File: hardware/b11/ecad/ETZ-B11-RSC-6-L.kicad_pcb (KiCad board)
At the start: 2 copper layers, 131.5 x 85.8 mm, 44 parts, among them SW1 Kailh_socket_PG1350, SW10 Kailh_socket_PG1350, SW11 Kailh_socket_PG1350, SW12 Kailh_socket_PG1350, SW13 Kailh_socket_PG1350, SW14 Kailh_socket_PG1350, SW15 Kailh_socket_PG1350, SW16 Kailh_socket_PG1350, SW17 Kailh_socket_PG1350, SW18 Kailh_socket_PG1350, SW19 Kailh_socket_PG1350, SW2 Kailh_socket_PG1350, SW20 Kailh_socket_PG1350, SW21 Kailh_socket_PG1350, SW22 Kailh_socket_PG1350, SW3 Kailh_socket_PG1350, SW4 Kailh_socket_PG1350, SW5 Kailh_socket_PG1350, SW6 Kailh_socket_PG1350, SW7 Kailh_socket_PG1350, SW8 Kailh_socket_PG1350, SW9 Kailh_socket_PG1350

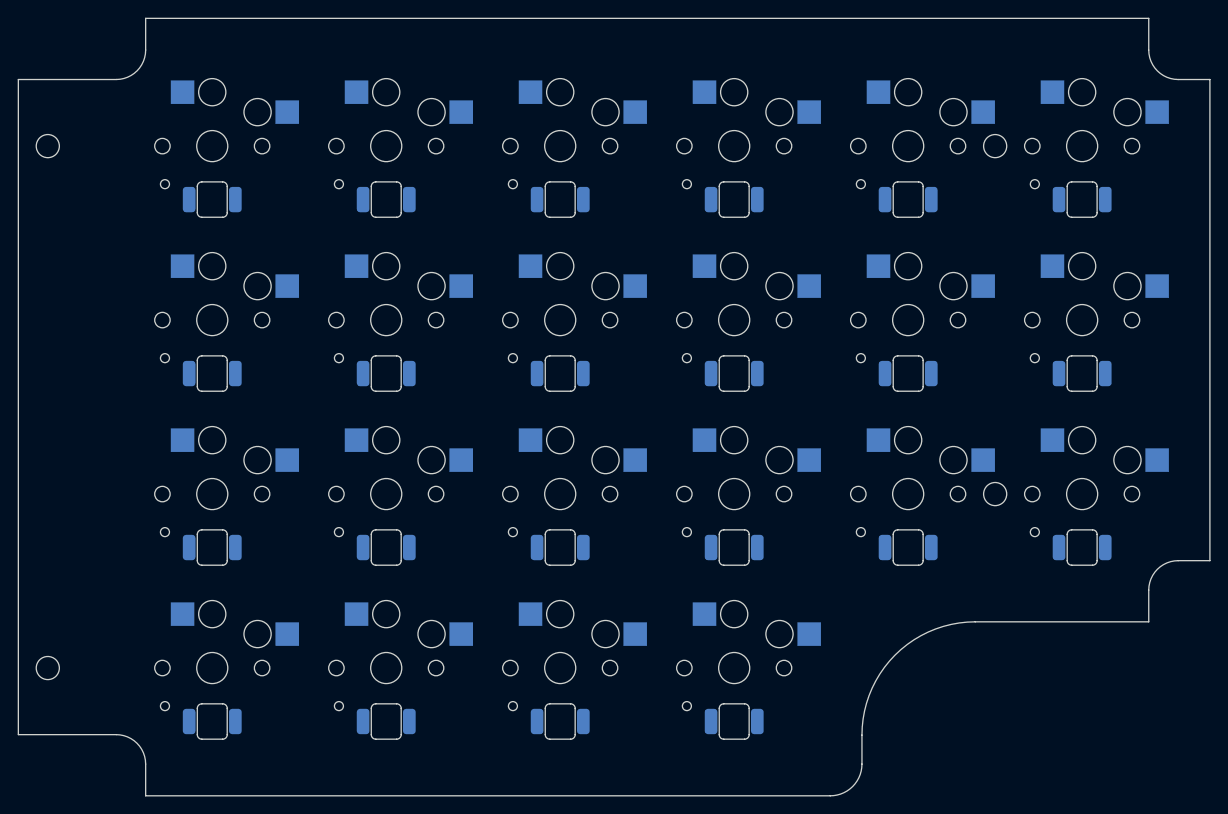
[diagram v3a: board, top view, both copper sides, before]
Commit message: fix(hardware/b11): fix switch socket placement, 3D models, and submodule pins
- Pin MX_V2 submodule to ab59b57 (before upstream "topside pads" change that
  moved SMD pads to F.Cu — old commit has correct B.Cu pads natively)
- Fix SWIG type-registry corruption in both switch placement scripts by
  pre-loading all footprint instances and caching pad refs before LoadBoard()
- Fix LP script: add make_patched_lib to rewrite Choc socket 3D model path
  to absolute path and convert old (at ...) inch offset to (offset ...) mm
  format — KiCad 9 was multiplying the old format by 25.4, placing model
  127mm off-center
- Regenerate all 8 carrier PCBs with updated board outlines (LSC-6 mounting
  hole positions) and correctly placed switches + LEDs

Co-Authored-By: Claude Sonnet 4.6 <noreply@anthropic.com>
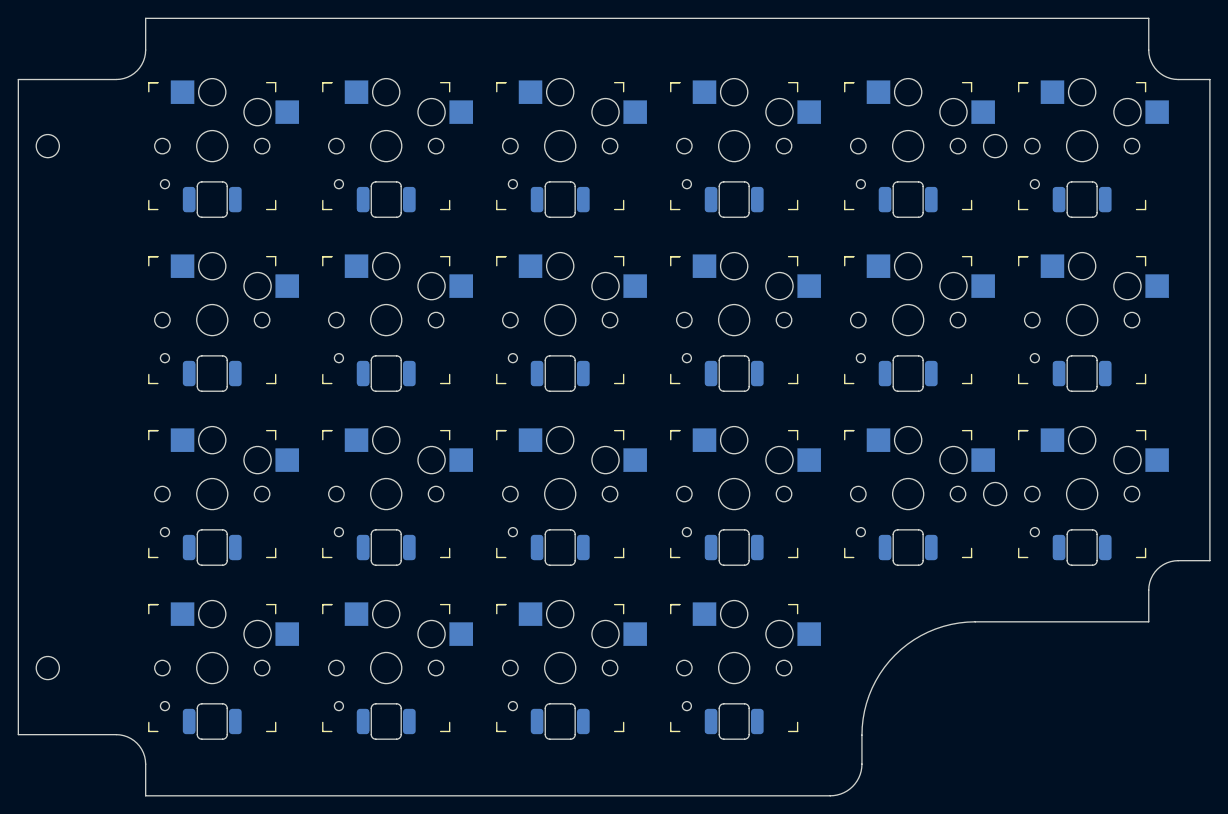
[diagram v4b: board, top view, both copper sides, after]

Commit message: fix(hardware/b11): adjust LED offset to 5.0mm and regenerate all carrier PCBs
Reduces south-facing LED offset from 5.9mm to 5.0mm (closer to the
standard 5.08mm switch-to-LED spacing). All 8 carrier PCBs regenerated.

Co-Authored-By: Claude Sonnet 4.6 <noreply@anthropic.com>
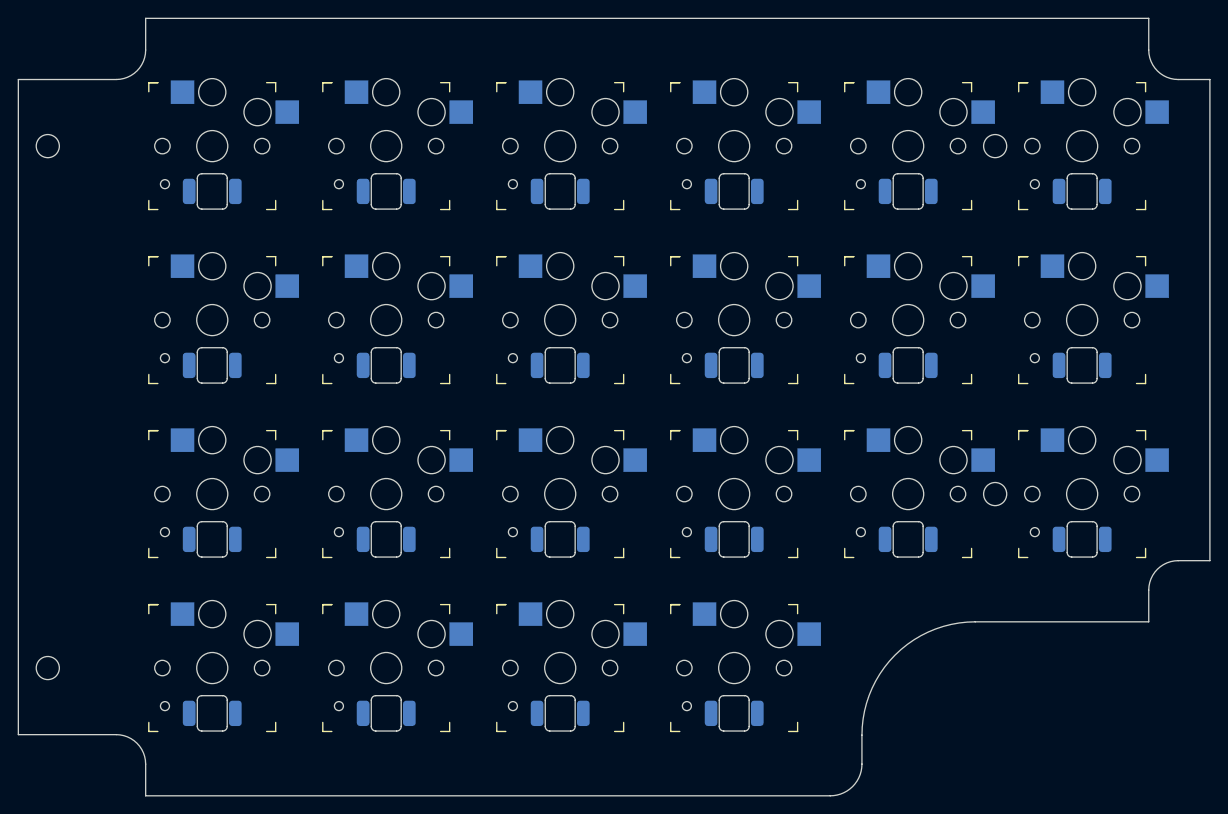
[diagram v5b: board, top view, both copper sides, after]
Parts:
- moved LED13 0.90 mm to (200.2, 116.7)
- moved LED14 0.90 mm to (180.9, 116.7)
- moved LED15 0.90 mm to (161.8, 116.7)
- moved LED16 0.90 mm to (142.6, 116.7)
- moved LED17 0.90 mm to (123.3, 116.7)
- moved LED18 0.90 mm to (104.2, 116.7)
- moved LED1 0.90 mm to (200.2, 78.3)
- moved LED10 0.90 mm to (142.6, 97.5)
- moved LED11 0.90 mm to (123.3, 97.5)
- moved LED12 0.90 mm to (104.2, 97.5)
- moved LED19 0.90 mm to (161.8, 135.9)
- moved LED2 0.90 mm to (180.9, 78.3)
- moved LED20 0.90 mm to (142.6, 135.9)
- moved LED21 0.90 mm to (123.3, 135.9)
- moved LED22 0.90 mm to (104.2, 135.9)
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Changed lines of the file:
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@@
 	(footprint "LED_SMD_6028_BackMount"
 		(layer "B.Cu")
-		(at 142.55 79.2)
+		(at 104.15 116.699999)
 		(descr "SMD 6028 back-paste reverse-mount LED, 5.88x2.80mm body, 3.20mm lens, slot 3.3x6.2mm")
 		(tags "LED SMD 6028 reverse-mount back-paste backlighting Choc")
-		(property "Reference" "LED4"
+		(property "Reference" "LED18"
 			(at 0 -2 0)
 			(layer "B.Fab")
@@
 	(footprint "LED_SMD_6028_BackMount"
 		(layer "B.Cu")
-		(at 200.15 98.4)
+		(at 200.15 97.5)
 		(descr "SMD 6028 back-paste reverse-mount LED, 5.88x2.80mm body, 3.20mm lens, slot 3.3x6.2mm")
 		(tags "LED SMD 6028 reverse-mount back-paste backlighting Choc")
@@
 	(footprint "LED_SMD_6028_BackMount"
 		(layer "B.Cu")
-		(at 123.35 117.6)
+		(at 161.75 116.699999)
 		(descr "SMD 6028 back-paste reverse-mount LED, 5.88x2.80mm body, 3.20mm lens, slot 3.3x6.2mm")
 		(tags "LED SMD 6028 reverse-mount back-paste backlighting Choc")
-		(property "Reference" "LED17"
+		(property "Reference" "LED15"
 			(at 0 -2 0)
 			(layer "B.Fab")
@@
 	(footprint "LED_SMD_6028_BackMount"
 		(layer "B.Cu")
-		(at 200.15 117.6)
+		(at 142.55 135.899999)
 		(descr "SMD 6028 back-paste reverse-mount LED, 5.88x2.80mm body, 3.20mm lens, slot 3.3x6.2mm")
 		(tags "LED SMD 6028 reverse-mount back-paste backlighting Choc")
-		(property "Reference" "LED13"
+		(property "Reference" "LED20"
 			(at 0 -2 0)
 			(layer "B.Fab")
@@
 	(footprint "LED_SMD_6028_BackMount"
 		(layer "B.Cu")
-		(at 180.95 98.4)
+		(at 161.75 78.3)
 		(descr "SMD 6028 back-paste reverse-mount LED, 5.88x2.80mm body, 3.20mm lens, slot 3.3x6.2mm")
 		(tags "LED SMD 6028 reverse-mount back-paste backlighting Choc")
-		(property "Reference" "LED8"
+		(property "Reference" "LED3"
 			(at 0 -2 0)
 			(layer "B.Fab")
@@
 	(footprint "LED_SMD_6028_BackMount"
 		(layer "B.Cu")
-		(at 123.35 98.4)
+		(at 161.75 97.5)
 		(descr "SMD 6028 back-paste reverse-mount LED, 5.88x2.80mm body, 3.20mm lens, slot 3.3x6.2mm")
 		(tags "LED SMD 6028 reverse-mount back-paste backlighting Choc")
-		(property "Reference" "LED11"
+		(property "Reference" "LED9"
 			(at 0 -2 0)
 			(layer "B.Fab")
@@
 	(footprint "LED_SMD_6028_BackMount"
 		(layer "B.Cu")
-		(at 104.15 136.799999)
+		(at 123.35 135.899999)
 		(descr "SMD 6028 back-paste reverse-mount LED, 5.88x2.80mm body, 3.20mm lens, slot 3.3x6.2mm")
 		(tags "LED SMD 6028 reverse-mount back-paste backlighting Choc")
-		(property "Reference" "LED22"
+		(property "Reference" "LED21"
 			(at 0 -2 0)
 			(layer "B.Fab")
@@
 	(footprint "LED_SMD_6028_BackMount"
 		(layer "B.Cu")
-		(at 142.55 117.6)
+		(at 104.15 135.899999)
 		(descr "SMD 6028 back-paste reverse-mount LED, 5.88x2.80mm body, 3.20mm lens, slot 3.3x6.2mm")
 		(tags "LED SMD 6028 reverse-mount back-paste backlighting Choc")
-		(property "Reference" "LED16"
+		(property "Reference" "LED22"
 			(at 0 -2 0)
 			(layer "B.Fab")
@@
 	(footprint "LED_SMD_6028_BackMount"
 		(layer "B.Cu")
-		(at 161.75 117.6)
+		(at 142.55 78.3)
 		(descr "SMD 6028 back-paste reverse-mount LED, 5.88x2.80mm body, 3.20mm lens, slot 3.3x6.2mm")
 		(tags "LED SMD 6028 reverse-mount back-paste backlighting Choc")
-		(property "Reference" "LED15"
+		(property "Reference" "LED4"
 			(at 0 -2 0)
 			(layer "B.Fab")
@@
 	(footprint "LED_SMD_6028_BackMount"
 		(layer "B.Cu")
-		(at 161.75 136.799999)
+		(at 180.95 116.699999)
 		(descr "SMD 6028 back-paste reverse-mount LED, 5.88x2.80mm body, 3.20mm lens, slot 3.3x6.2mm")
 		(tags "LED SMD 6028 reverse-mount back-paste backlighting Choc")
-		(property "Reference" "LED19"
+		(property "Reference" "LED14"
 			(at 0 -2 0)
 			(layer "B.Fab")
@@
 	(footprint "LED_SMD_6028_BackMount"
 		(layer "B.Cu")
-		(at 161.75 98.4)
+		(at 180.95 97.5)
 		(descr "SMD 6028 back-paste reverse-mount LED, 5.88x2.80mm body, 3.20mm lens, slot 3.3x6.2mm")
 		(tags "LED SMD 6028 reverse-mount back-paste backlighting Choc")
-		(property "Reference" "LED9"
+		(property "Reference" "LED8"
 			(at 0 -2 0)
 			(layer "B.Fab")
@@
 	(footprint "LED_SMD_6028_BackMount"
 		(layer "B.Cu")
-		(at 142.55 136.799999)
+		(at 123.35 97.5)
 		(descr "SMD 6028 back-paste reverse-mount LED, 5.88x2.80mm body, 3.20mm lens, slot 3.3x6.2mm")
 		(tags "LED SMD 6028 reverse-mount back-paste backlighting Choc")
-		(property "Reference" "LED20"
+		(property "Reference" "LED11"
 			(at 0 -2 0)
 			(layer "B.Fab")
@@
 	(footprint "LED_SMD_6028_BackMount"
 		(layer "B.Cu")
-		(at 180.95 117.6)
+		(at 180.95 78.3)
 		(descr "SMD 6028 back-paste reverse-mount LED, 5.88x2.80mm body, 3.20mm lens, slot 3.3x6.2mm")
 		(tags "LED SMD 6028 reverse-mount back-paste backlighting Choc")
-		(property "Reference" "LED14"
+		(property "Reference" "LED2"
 			(at 0 -2 0)
 			(layer "B.Fab")
@@
 	(footprint "LED_SMD_6028_BackMount"
 		(layer "B.Cu")
-		(at 161.75 79.2)
+		(at 142.55 97.5)
 		(descr "SMD 6028 back-paste reverse-mount LED, 5.88x2.80mm body, 3.20mm lens, slot 3.3x6.2mm")
 		(tags "LED SMD 6028 reverse-mount back-paste backlighting Choc")
-		(property "Reference" "LED3"
+		(property "Reference" "LED10"
 			(at 0 -2 0)
 			(layer "B.Fab")
@@
 	(footprint "LED_SMD_6028_BackMount"
 		(layer "B.Cu")
-		(at 123.35 136.799999)
+		(at 161.75 135.899999)
 		(descr "SMD 6028 back-paste reverse-mount LED, 5.88x2.80mm body, 3.20mm lens, slot 3.3x6.2mm")
 		(tags "LED SMD 6028 reverse-mount back-paste backlighting Choc")
-		(property "Reference" "LED21"
+		(property "Reference" "LED19"
 			(at 0 -2 0)
 			(layer "B.Fab")
@@
 	(footprint "LED_SMD_6028_BackMount"
 		(layer "B.Cu")
-		(at 142.55 98.4)
+		(at 200.15 116.699999)
 		(descr "SMD 6028 back-paste reverse-mount LED, 5.88x2.80mm body, 3.20mm lens, slot 3.3x6.2mm")
 		(tags "LED SMD 6028 reverse-mount back-paste backlighting Choc")
-		(property "Reference" "LED10"
+		(property "Reference" "LED13"
 			(at 0 -2 0)
 			(layer "B.Fab")
@@
 	(footprint "LED_SMD_6028_BackMount"
 		(layer "B.Cu")
-		(at 104.15 98.4)
+		(at 200.15 78.3)
 		(descr "SMD 6028 back-paste reverse-mount LED, 5.88x2.80mm body, 3.20mm lens, slot 3.3x6.2mm")
 		(tags "LED SMD 6028 reverse-mount back-paste backlighting Choc")
-		(property "Reference" "LED12"
+		(property "Reference" "LED1"
 			(at 0 -2 0)
 			(layer "B.Fab")
@@
 	(footprint "LED_SMD_6028_BackMount"
 		(layer "B.Cu")
-		(at 200.15 79.2)
+		(at 104.15 97.5)
 		(descr "SMD 6028 back-paste reverse-mount LED, 5.88x2.80mm body, 3.20mm lens, slot 3.3x6.2mm")
 		(tags "LED SMD 6028 reverse-mount back-paste backlighting Choc")
-		(property "Reference" "LED1"
+		(property "Reference" "LED12"
 			(at 0 -2 0)
 			(layer "B.Fab")
@@
 	(footprint "LED_SMD_6028_BackMount"
 		(layer "B.Cu")
-		(at 123.35 79.2)
+		(at 123.35 78.3)
 		(descr "SMD 6028 back-paste reverse-mount LED, 5.88x2.80mm body, 3.20mm lens, slot 3.3x6.2mm")
 		(tags "LED SMD 6028 reverse-mount back-paste backlighting Choc")
@@
 	(footprint "LED_SMD_6028_BackMount"
 		(layer "B.Cu")
-		(at 104.15 79.2)
+		(at 123.35 116.699999)
 		(descr "SMD 6028 back-paste reverse-mount LED, 5.88x2.80mm body, 3.20mm lens, slot 3.3x6.2mm")
 		(tags "LED SMD 6028 reverse-mount back-paste backlighting Choc")
-		(property "Reference" "LED6"
+		(property "Reference" "LED17"
 			(at 0 -2 0)
 			(layer "B.Fab")
@@
 	(footprint "LED_SMD_6028_BackMount"
 		(layer "B.Cu")
-		(at 104.15 117.6)
+		(at 104.15 78.3)
 		(descr "SMD 6028 back-paste reverse-mount LED, 5.88x2.80mm body, 3.20mm lens, slot 3.3x6.2mm")
 		(tags "LED SMD 6028 reverse-mount back-paste backlighting Choc")
-		(property "Reference" "LED18"
+		(property "Reference" "LED6"
 			(at 0 -2 0)
 			(layer "B.Fab")
@@
 	(footprint "LED_SMD_6028_BackMount"
 		(layer "B.Cu")
-		(at 180.95 79.2)
+		(at 142.55 116.699999)
 		(descr "SMD 6028 back-paste reverse-mount LED, 5.88x2.80mm body, 3.20mm lens, slot 3.3x6.2mm")
 		(tags "LED SMD 6028 reverse-mount back-paste backlighting Choc")
-		(property "Reference" "LED2"
+		(property "Reference" "LED16"
 			(at 0 -2 0)
 			(layer "B.Fab")
